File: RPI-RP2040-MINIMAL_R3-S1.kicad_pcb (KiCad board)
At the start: 2 copper layers, 65 x 46.7 mm, 31 parts, among them J3 Conn_01x04_Pin, J4 Conn_01x04_Socket, P1 USB_C_Plug_USB2.0, U1 NCP1117ST33T3G, U2 W25Q128JVSIQ, U3 RP2040, X1 12MHz

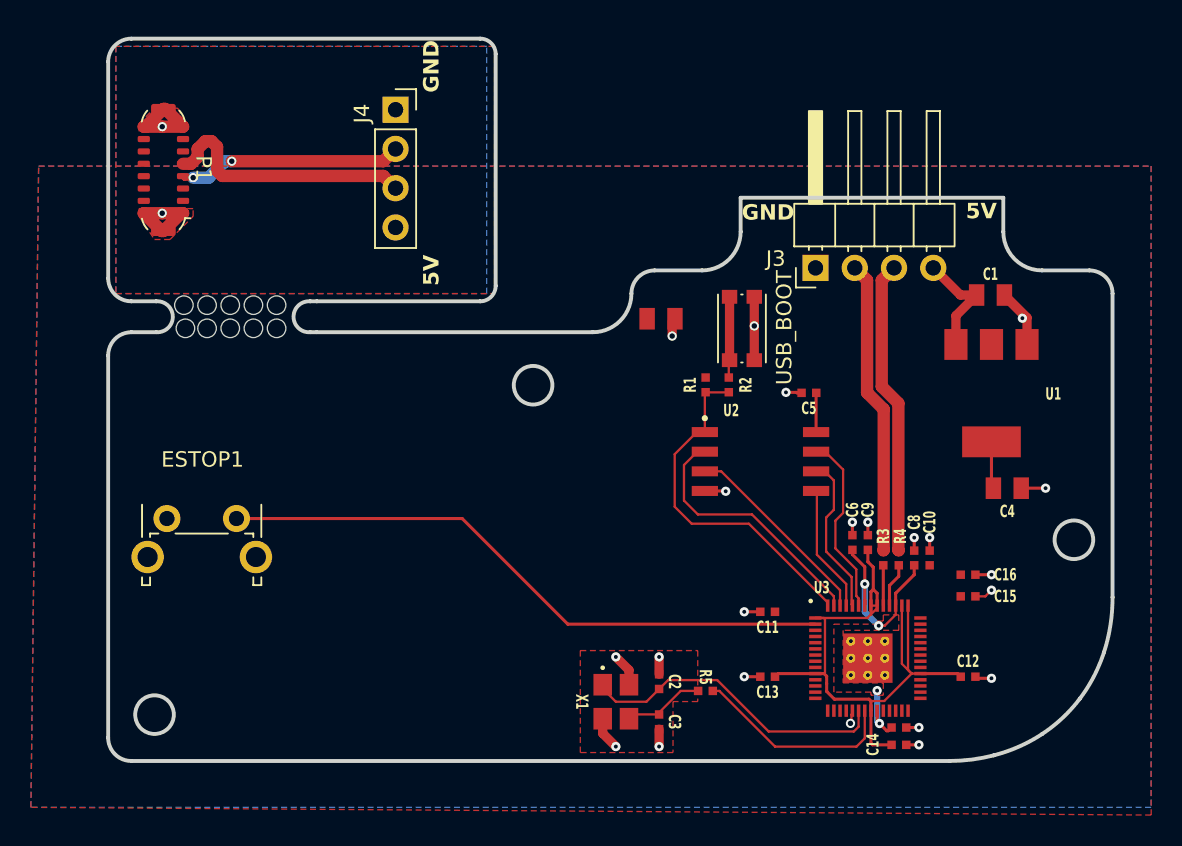
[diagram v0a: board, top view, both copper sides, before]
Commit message: switch to 2mb flash + debug port
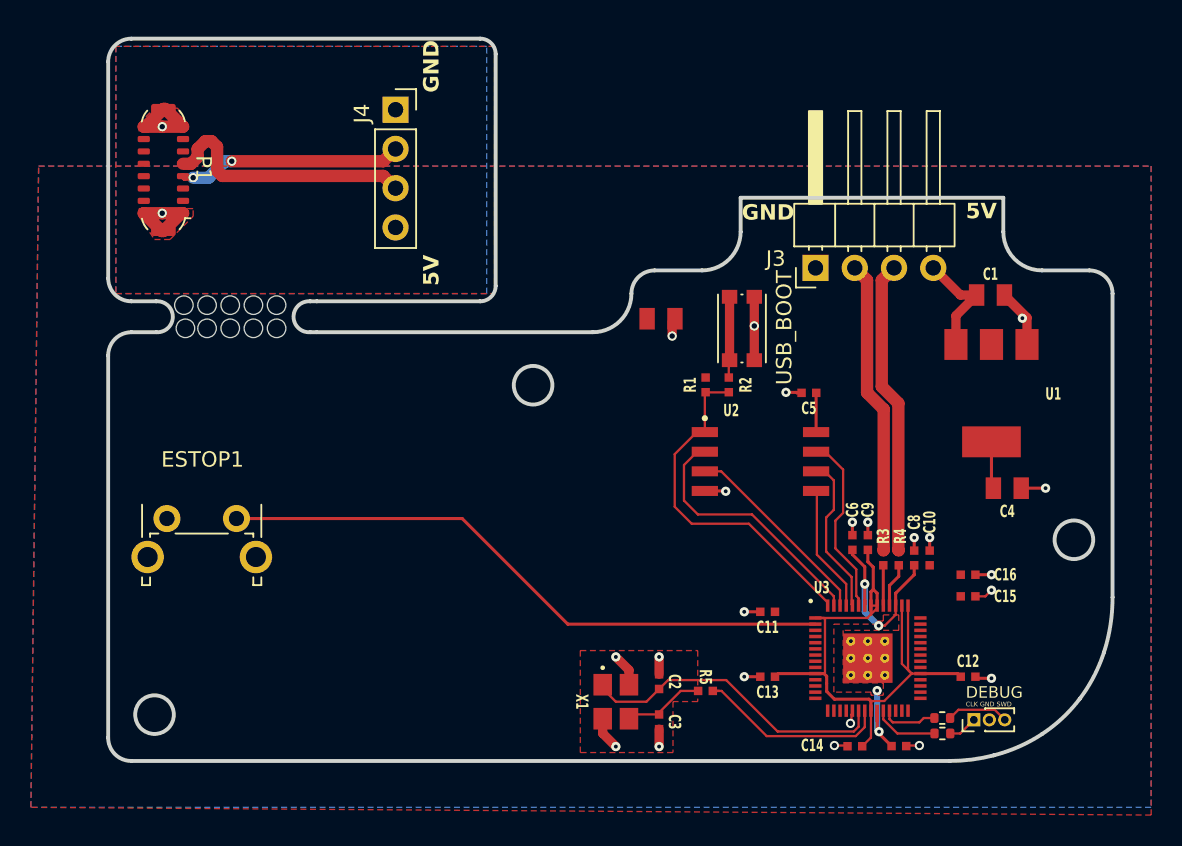
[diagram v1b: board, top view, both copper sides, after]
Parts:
- added J1: Conn_01x03_Socket, Connector_PinHeader_1.00mm:PinHeader_1x03_P1.00mm_Vertical, F.Cu at (106.5, 104.3)
- added R6: 100, Resistor_SMD:R_0402_1005Metric, F.Cu at (104.5, 105.2)
- added R7: 100, Resistor_SMD:R_0402_1005Metric, F.Cu at (104.5, 104.2)
- moved C14 2.85 mm to (98.8, 106.0), turned to 180 degrees
- moved C7 1.20 mm to (101.7, 106.0)
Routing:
- net /SWCLK: track 0.00 -> 4.25 mm
- net Net-(J1-Pin_3): track 0.00 -> 4.03 mm
- net /SWD: track 0.00 -> 3.65 mm
- net +1V1: track 16.2 -> 18.1 mm
- net Net-(J1-Pin_1): track 0.00 -> 1.89 mm
- net +3V3: track 48.0 -> 47.1 mm
- net /XOUT: track 13.3 -> 12.7 mm
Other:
- board text added: "CLK GND SWD"
- board text added: "DEBUG"
